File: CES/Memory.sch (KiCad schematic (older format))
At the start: 8 parts, among them U1101 SST39SF020, U1102 SST39SF020, U1103 IS61C256, U1104 IS61C256

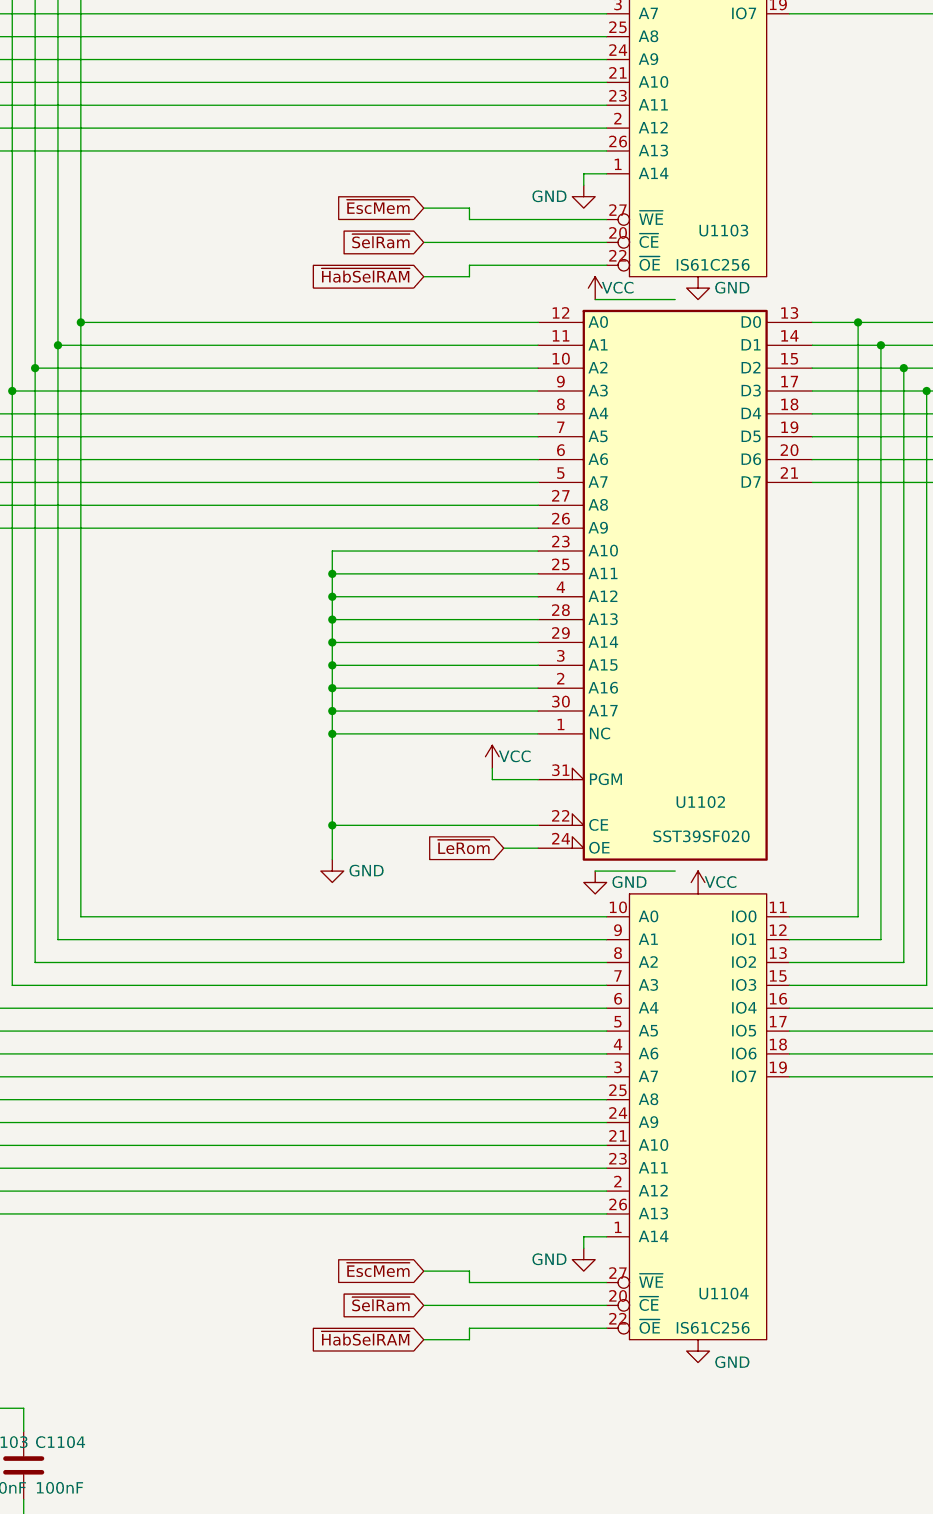
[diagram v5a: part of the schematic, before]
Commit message: Correcting footprints errors
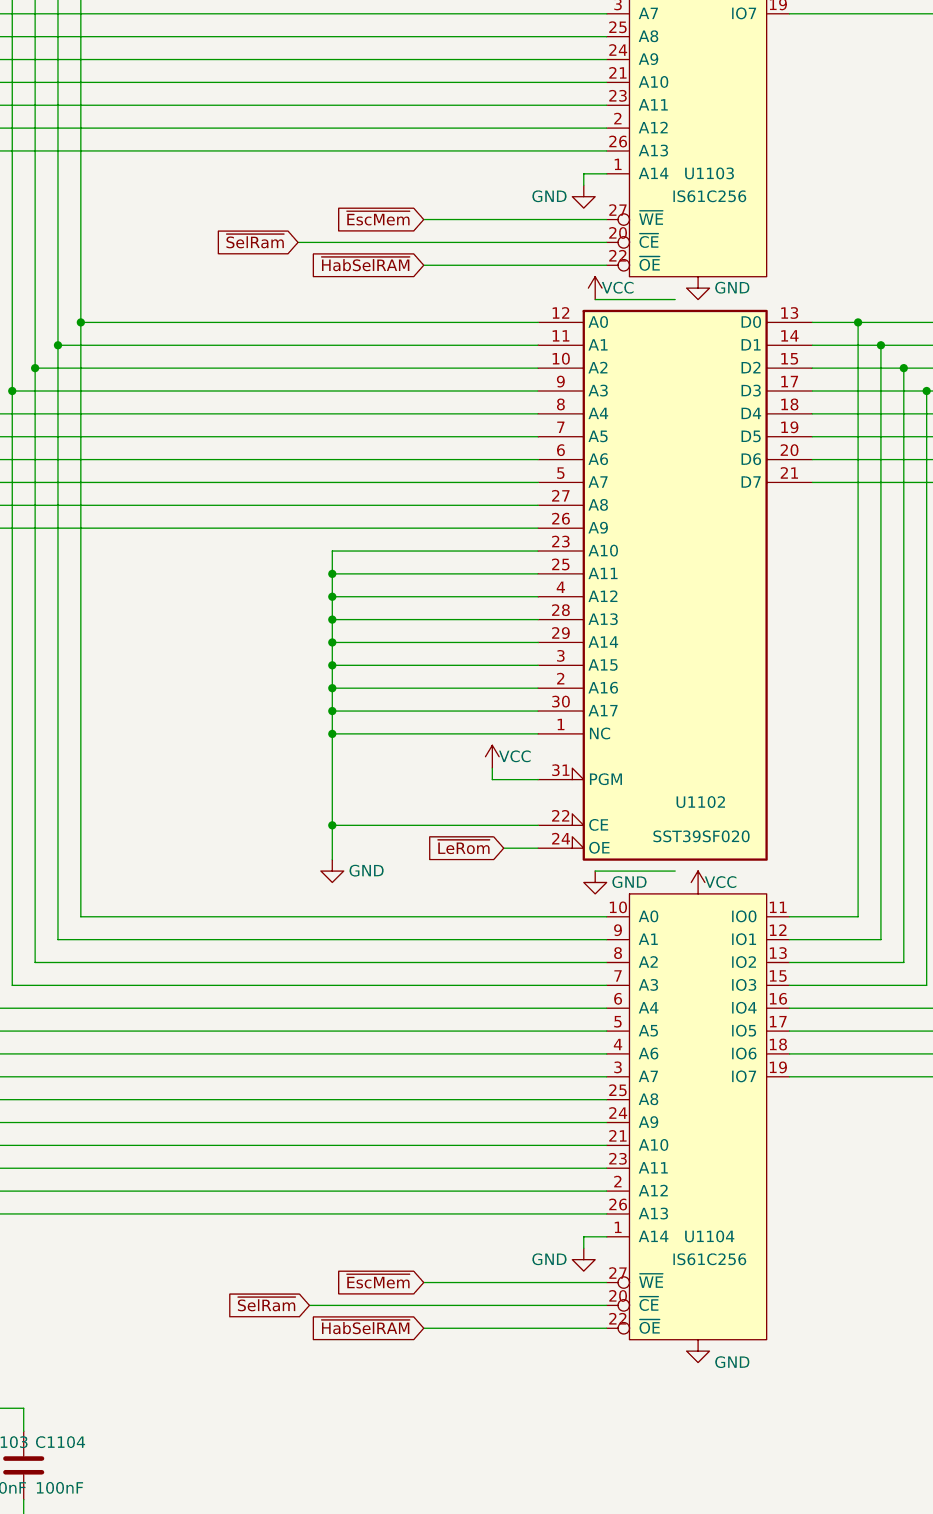
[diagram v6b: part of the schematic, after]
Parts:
- C1101, C1102, C1103, C1104: footprint Capacitor_THT:CP_Radial_D5.0mm_P2.50mm -> Capacitor_THT:C_Disc_D4.3mm_W1.9mm_P5.00mm
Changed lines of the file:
@@
-$EndComp
-$Comp
-L CES:IS61C256 U1103
-U 1 1 60841D0E
-P 4850 4200
-F 0 "U1103" H 4850 3450 50  0000 L CNN
-F 1 "IS61C256" H 4750 3300 50  0000 L CNN
-F 2 "Package_DIP:DIP-28_W7.62mm" H 1900 2750 50  0001 C CNN
-F 3 "" H 1900 2750 50  0001 C CNN
-	1    4850 4200
-	1    0    0    -1
 $EndComp
 $Comp
@@
 F 0 "C1101" H 1150 10450 50  0000 L CNN
 F 1 "100nF" H 1150 10250 50  0000 L CNN
-F 2 "Capacitor_THT:CP_Radial_D5.0mm_P2.50mm" H 1138 10200 50  0001 C CNN
+F 2 "Capacitor_THT:C_Disc_D4.3mm_W1.9mm_P5.00mm" H 1138 10200 50  0001 C CNN
 F 3 "~" H 1100 10350 50  0001 C CNN
 	1    1100 10350
@@
 F 0 "C1102" H 1450 10450 50  0000 L CNN
 F 1 "100nF" H 1450 10250 50  0000 L CNN
-F 2 "Capacitor_THT:CP_Radial_D5.0mm_P2.50mm" H 1438 10200 50  0001 C CNN
+F 2 "Capacitor_THT:C_Disc_D4.3mm_W1.9mm_P5.00mm" H 1438 10200 50  0001 C CNN
 F 3 "~" H 1400 10350 50  0001 C CNN
 	1    1400 10350
@@
 F 0 "C1103" H 1700 10450 50  0000 L CNN
 F 1 "100nF" H 1700 10250 50  0000 L CNN
-F 2 "Capacitor_THT:CP_Radial_D5.0mm_P2.50mm" H 1688 10200 50  0001 C CNN
+F 2 "Capacitor_THT:C_Disc_D4.3mm_W1.9mm_P5.00mm" H 1688 10200 50  0001 C CNN
 F 3 "~" H 1650 10350 50  0001 C CNN
 	1    1650 10350
@@
 F 0 "C1104" H 1950 10450 50  0000 L CNN
 F 1 "100nF" H 1950 10250 50  0000 L CNN
-F 2 "Capacitor_THT:CP_Radial_D5.0mm_P2.50mm" H 1938 10200 50  0001 C CNN
+F 2 "Capacitor_THT:C_Disc_D4.3mm_W1.9mm_P5.00mm" H 1938 10200 50  0001 C CNN
 F 3 "~" H 1900 10350 50  0001 C CNN
 	1    1900 10350
@@
 	3250 7700 3250 7550
 Connection ~ 3250 7550
-Text GLabel 3650 4850 0    50   Input ~ 0
+Text GLabel 3650 4900 0    50   Input ~ 0
 ~EscMem
-Text GLabel 3650 5000 0    50   Input ~ 0
+Text GLabel 3100 5000 0    50   Input ~ 0
 ~SelRam
-Text GLabel 3650 5150 0    50   Input ~ 0
+Text GLabel 3650 5100 0    50   Input ~ 0
 ~HabSelRAM
 Wire Wire Line
-	3650 5000 4450 5000
-Wire Wire Line
-	4450 4900 3850 4900
-Wire Wire Line
-	3850 4900 3850 4850
-Wire Wire Line
-	3850 4850 3650 4850
-Wire Wire Line
-	3650 5150 3850 5150
-Wire Wire Line
-	3850 5150 3850 5100
-Wire Wire Line
-	3850 5100 4450 5100
-Text GLabel 3650 9500 0    50   Input ~ 0
+	3100 5000 4450 5000
+Text GLabel 3650 9550 0    50   Input ~ 0
 ~EscMem
-Text GLabel 3650 9650 0    50   Input ~ 0
+Text GLabel 3150 9650 0    50   Input ~ 0
 ~SelRam
-Text GLabel 3650 9800 0    50   Input ~ 0
+Text GLabel 3650 9750 0    50   Input ~ 0
 ~HabSelRAM
 Wire Wire Line
-	3650 9650 4450 9650
-Wire Wire Line
-	4450 9550 3850 9550
-Wire Wire Line
-	3850 9550 3850 9500
-Wire Wire Line
-	3850 9500 3650 9500
-Wire Wire Line
-	3650 9800 3850 9800
-Wire Wire Line
-	3850 9800 3850 9750
-Wire Wire Line
-	3850 9750 4450 9750
+	3150 9650 4450 9650
 $Comp
 L power:GND #PWR01111
@@
 $EndComp
 $Comp
-L CES:IS61C256 U1104
-U 1 1 6083E55E
-P 4850 8850
-F 0 "U1104" H 4850 8100 50  0000 L CNN
-F 1 "IS61C256" H 4750 7950 50  0000 L CNN
-F 2 "Package_DIP:DIP-28_W7.62mm" H 1900 7400 50  0001 C CNN
-F 3 "" H 1900 7400 50  0001 C CNN
-	1    4850 8850
-	1    0    0    -1
-$EndComp
-$Comp
 L power:GND #PWR01116
 U 1 1 60F39577
@@
 Wire Wire Line
 	4400 7750 4750 7750
+Wire Wire Line
+	3650 9750 4450 9750
+Wire Wire Line
+	3650 9550 4450 9550
+Wire Wire Line
+	3650 5100 4450 5100
+Wire Wire Line
+	3650 4900 4450 4900
+$Comp
+L CES:IS61C256 U1104
+U 1 1 60B72304
+P 4850 8850
+F 0 "U1104" H 4900 8350 50  0000 C CNN
+F 1 "IS61C256" H 4900 8250 50  0000 C CNN
+F 2 "Package_DIP:DIP-28_W7.62mm" H 1900 7400 50  0001 C CNN
+F 3 "https://www.issi.com/WW/pdf/61C256AH.pdf" H 1900 7400 50  0001 C CNN
+	1    4850 8850
+	1    0    0    -1
+$EndComp
+$Comp
+L CES:IS61C256 U1103
+U 1 1 60B7462F
+P 4850 4200
+F 0 "U1103" H 4900 3700 50  0000 C CNN
+F 1 "IS61C256" H 4900 3600 50  0000 C CNN
+F 2 "Package_DIP:DIP-28_W7.62mm" H 1900 2750 50  0001 C CNN
+F 3 "https://www.issi.com/WW/pdf/61C256AH.pdf" H 1900 2750 50  0001 C CNN
+	1    4850 4200
+	1    0    0    -1
+$EndComp
 $EndSCHEMATC
